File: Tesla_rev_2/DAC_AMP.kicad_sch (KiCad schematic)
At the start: 39 parts, among them K1 G6EU, Q3 BC817, Q4 BC817, U5 PCM5102A, U6 MCP6497, U7 TPA0211

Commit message: revision 3
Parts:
- removed C18, C20, C27: 100nF, Capacitor_SMD:C_0805_2012Metric_Pad1.18x1.45mm_HandSolder, symbol Device:C
- removed C19, C23, C26, C29: 10uF, symbol Device:C_Polarized
- removed C30: 470nF, symbol Device:C
- removed C35: 10uF, Capacitor_SMD:CP_Elec_6.3x7.7, symbol Device:C_Polarized
- removed C36: 100nF, Capacitor_SMD:CP_Elec_4x5.4, symbol Device:C_Polarized
- removed Q4: BC817, Package_TO_SOT_SMD:SOT-23, symbol Transistor_BJT:BC817
- removed R11: 470, symbol Device:R_Small
- removed R12: 3.3K, symbol Device:R_Small
- removed R14: 0R, symbol Device:R_Small
- removed R20: 1K, symbol Device:R_Small
- removed R21: 20K, symbol Device:R_Small
- removed RV1: 5K, symbol Device:R_Potentiometer
- added C15, C21, C3, C4, C6: 10uF, symbol Device:C
- added R17, R18: TBD, symbol Device:R_Small
- added R8: 470, symbol Device:R_Small
- added R9: 3.3K, symbol Device:R_Small
- added TP1, TP2: TestPoint, symbol Connector:TestPoint
- C17: renamed from C25; Part_num MKS2C032201B00KSSD -> (none)
- C18: renamed from C33; value 0.47uF -> 470nF
- C19: renamed from C28; Part_num MKS2C032201B00KSSD -> (none)
- C20: renamed from C34; value 0.47uF -> 470nF
- C24: value 0.1uF -> 100nF
- R10: renamed from R13; Part_num MMA02040C3001FB000 -> (none)
- R14: renamed from R19; Part_num MMA02040E1002BB300 -> (none)
- R5: renamed from R18; Part_num MMU01020C7501FB300 -> (none)
- R7: renamed from R10; Part_num MMB02070C4700FB200 -> (none)
- renumbered C21 to C10, C22 to C11, C31 to C2, C32 to C25, D2 to D3, Q3 to Q1, R15 to R19, R16 to R3, R17 to R4, U6 to U2, U5 to U3, U7 to U5
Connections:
- net I2S.SCK is gone; now on net GND: U3.12 (SCK)
- net XSMT is gone; now on net +3.3V: U3.17 (XSMT)
- net ~{SD} is gone; now on net AMP_SD: U5.2 (~{SD})
- net +3.3V: now also C3.1, C4.1, C6.1
- net +5V: now also C24.1, C21.1
- net DAC_LDOO: now also C15.1; no longer C24.1
- net DAC_L/R_OUT: now also R9.2, TP2.1
- net GND: now also C15.2, C21.2, C3.2, C4.2, C6.2, R18.2
- net OP_AMP_BIAS: now also TP1.1
- net OUTL_LPF: now also R9.1
- net OUTR: now also R8.1
- net OUTR_LPF: now also R8.2
- net RADIO_AUDIO_IN: now also R17.1
- net at K1.10: now also R17.2, R18.1
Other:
- note removed: "SCK - System clock = sample freq. * 128 BCK - Bit clock / sample freq. = 96KHz"
- moved on the sheet: C10, C11, C17, C18, C19, C2, C20, C25, D3, K1, Q1, R10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

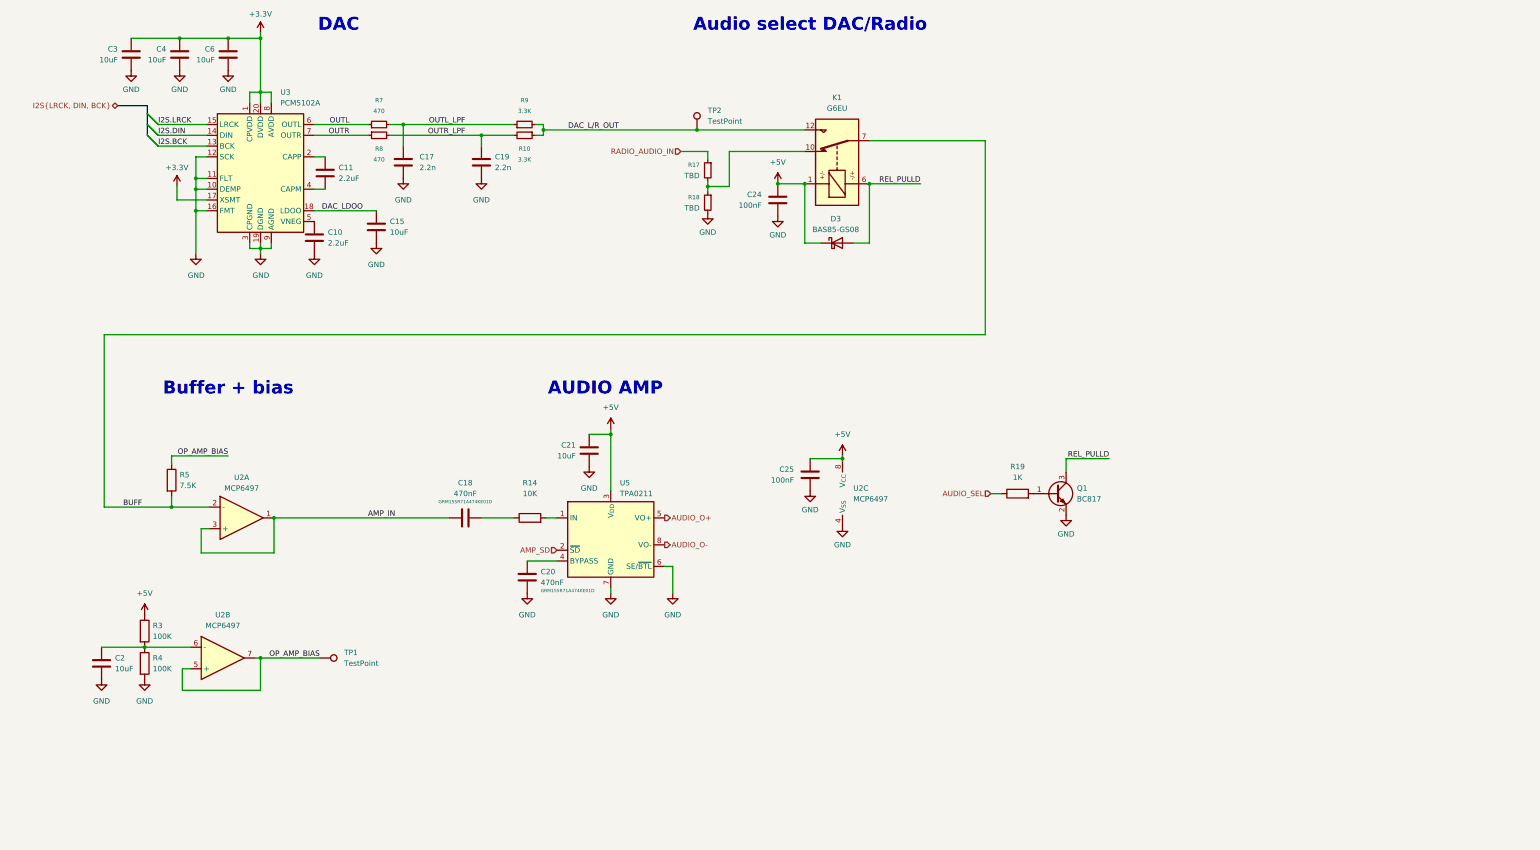
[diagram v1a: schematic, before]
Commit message: Rev 2.3, schematic and footprint fixes, prepared for layout
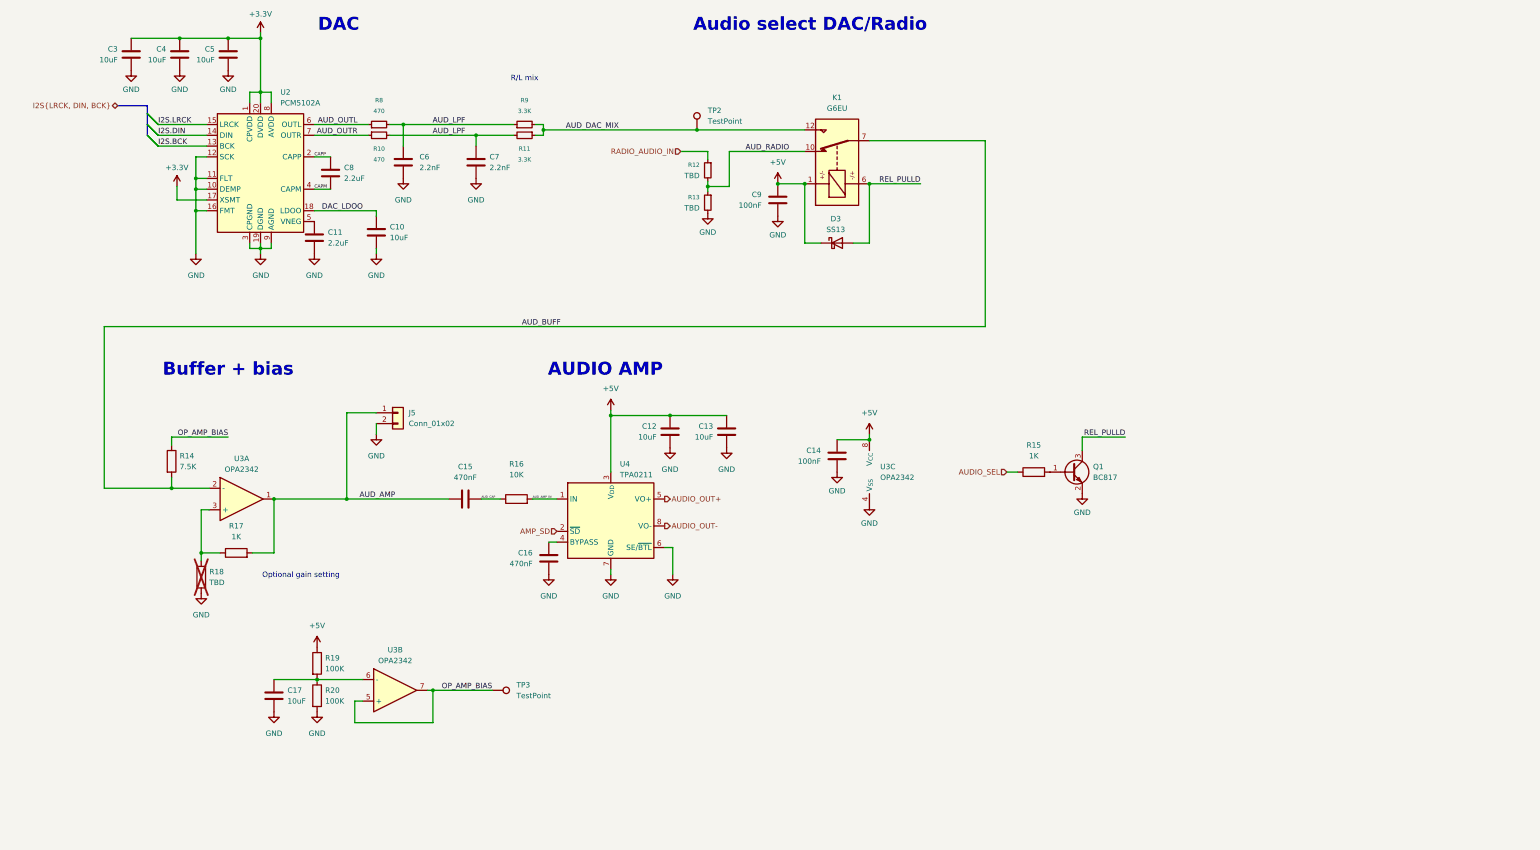
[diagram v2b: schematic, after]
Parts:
- removed D3: BAS85-GS08, Diode_SMD:D_MiniMELF, symbol Device:D_Schottky
- removed U2: MCP6497, Package_SO:SOIC-8_3.9x4.9mm_P1.27mm, symbol Tesla_sextant_BT_Library:MCP6497
- added C12: 10uF, Capacitor_SMD:C_0805_2012Metric, symbol Device:C
- added D3: SS13, Package_TO_SOT_SMD:SOT-323_SC-70, symbol Diode:SS13
- added J5: Conn_01x02, Tesla_Library:Conn_Solder_1x02_SMD, symbol Connector_Generic:Conn_01x02
- added R17: 1K, Capacitor_SMD:C_0805_2012Metric, symbol Device:R
- added R18: TBD, Capacitor_SMD:C_0805_2012Metric, symbol Device:R
- added U3: OPA2342, Package_SO:SOIC-8_3.9x4.9mm_P1.27mm, symbol Tesla_sextant_BT_Library:OPA2342
- C10: renamed from C15; footprint (none) -> Capacitor_SMD:C_0805_2012Metric
- C13: renamed from C21; footprint (none) -> Capacitor_SMD:C_0805_2012Metric
- C15: renamed from C18; footprint (none) -> Capacitor_SMD:C_0805_2012Metric; Part_num GRM155R71A474KE01D -> (none)
- C16: renamed from C20; footprint (none) -> Capacitor_SMD:C_0805_2012Metric; Part_num GRM155R71A474KE01D -> (none)
- C17: renamed from C2; footprint (none) -> Capacitor_SMD:C_0805_2012Metric
- C3, C4, R9: footprint (none) -> Capacitor_SMD:C_0805_2012Metric
- C5: renamed from C6; footprint (none) -> Capacitor_SMD:C_0805_2012Metric
- C6: renamed from C17; value 2.2n -> 2.2nF; footprint (none) -> Capacitor_SMD:C_0805_2012Metric
- C7: renamed from C19; value 2.2n -> 2.2nF; footprint (none) -> Capacitor_SMD:C_0805_2012Metric
- C8: renamed from C11; footprint (none) -> Capacitor_SMD:C_0805_2012Metric
- R10: renamed from R8; footprint (none) -> Capacitor_SMD:C_0805_2012Metric
- R11: renamed from R10; footprint (none) -> Capacitor_SMD:C_0805_2012Metric
- R12: renamed from R17; footprint (none) -> Resistor_SMD:R_0805_2012Metric
- R13: renamed from R18; footprint (none) -> Resistor_SMD:R_0805_2012Metric
- R14: renamed from R5; footprint (none) -> Capacitor_SMD:C_0805_2012Metric
- R15: renamed from R19; footprint (none) -> Capacitor_SMD:C_0805_2012Metric
- R16: renamed from R14; footprint (none) -> Capacitor_SMD:C_0805_2012Metric
- R19: renamed from R3; footprint (none) -> Capacitor_SMD:C_0805_2012Metric
- R20: renamed from R4; footprint (none) -> Capacitor_SMD:C_0805_2012Metric
- R8: renamed from R7; footprint (none) -> Capacitor_SMD:C_0805_2012Metric
- TP2: footprint (none) -> TestPoint:TestPoint_Pad_D2.5mm; now left out of the parts list
- TP3: renamed from TP1; footprint (none) -> TestPoint:TestPoint_Pad_D2.5mm; now left out of the parts list
- renumbered C10 to C11, C25 to C14, C24 to C9, U3 to U2, U5 to U4
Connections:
- net OUTR_LPF is gone; now on net AUD_LPF: C7.1, R10.2, R11.2
- net +5V: now also C12.1, D3.1 (K), U3.8 (V_{CC})
- net GND: now also C12.2, J5.2 (Pin_2), R18.1, U3.4 (V_{SS})
- net OP_AMP_BIAS: now also U3.5 (+), U3.7
- net REL_PULLD: now also D3.2 (A)
- net CAPP: now reaches C8.1, U2.2 (CAPP)
- net CAPM: now reaches C8.2, U2.4 (CAPM)
- net at C17.1, R19.2, R20.1: now also U3.6 (-)
- net AUD_RADIO: now reaches K1.10, R12.2, R13.1
- net AUD_AMP_IN: now reaches R16.2, U4.1 (IN)
- net AUD_CAP: now reaches C15.2, R16.1
- net AMP_IN renamed AUD_AMP
- net AUD_AMP: now also J5.1 (Pin_1), R17.2, U3.1
- net AUDIO_O+ renamed AUDIO_OUT+
- net AUDIO_O- renamed AUDIO_OUT-
- net BUFF renamed AUD_BUFF
- net AUD_BUFF: now also U3.2 (-)
- net DAC_L/R_OUT renamed AUD_DAC_MIX
- net OUTL renamed AUD_OUTL
- net OUTL_LPF renamed AUD_LPF
- net OUTR renamed AUD_OUTR
- new net: R17.1, R18.2, U3.3 (+)
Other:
- note added: "Optional gain setting"
- note added: "R/L mix"
- title: Tesla sextant BT -> Tesla sextant BT DAC
- moved on the sheet: C10, C13, C14, C15, C16, C17, C7, C8, Q1, R14, R15, R16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

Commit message: added PCB layou
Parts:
- removed D3: SS13, Package_TO_SOT_SMD:SOT-323_SC-70, symbol Diode:SS13
- removed J5: Conn_01x02, Tesla_Library:Conn_Solder_1x02_SMD, symbol Connector_Generic:Conn_01x02
- added C41: TBD, Capacitor_SMD:C_0805_2012Metric, symbol Device:C
- added D3: B220, Diode_SMD:D_SMB, symbol Diode:B220
- C11, C14, C9: footprint Capacitor_SMD:C_0805_2012Metric_Pad1.18x1.45mm_HandSolder -> Capacitor_SMD:C_0805_2012Metric
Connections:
- net +5V: now also D3.1 (K)
- net AUD_AMP: now also U3.7; no longer U3.1
- net AUD_BUFF: now also U3.6 (-); no longer U3.2 (-)
- net AUD_RADIO: now also C41.1
- net GND: now also C41.2
- net OP_AMP_BIAS: now also U3.1, U3.3 (+); no longer U3.5 (+), U3.7
- net REL_PULLD: now also D3.2 (A)
- net BUFF_FB: now reaches R17.1, R18.2
- net BUFF_FB: now also U3.5 (+); no longer U3.3 (+)
- net DIV_2.5V: now reaches C17.1, R19.2, R20.1
- net DIV_2.5V: now also U3.2 (-); no longer U3.6 (-)
- net AUDIO_SEL renamed INPUT_SEL
- net AUD_LPF renamed AUD_LPF_L
- net AUD_LPF_L: no longer C7.1, R10.2, R11.2
- new net AUD_LPF_R: C7.1, R10.2, R11.2
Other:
- moved on the sheet: U3A, U3B
